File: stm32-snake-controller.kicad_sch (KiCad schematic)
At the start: 48 parts, among them J101 Barrel_Jack_MountingPin, J101 Tag Connector, J103 JST 2.54 Header, Q101 AO3501A, SW106 SW_Push, U101 STM32F446RCTx, U102 USBLC6-2SC6, U104 M24C64-RMN, Y101 16MHz, Y103 32.768kHz

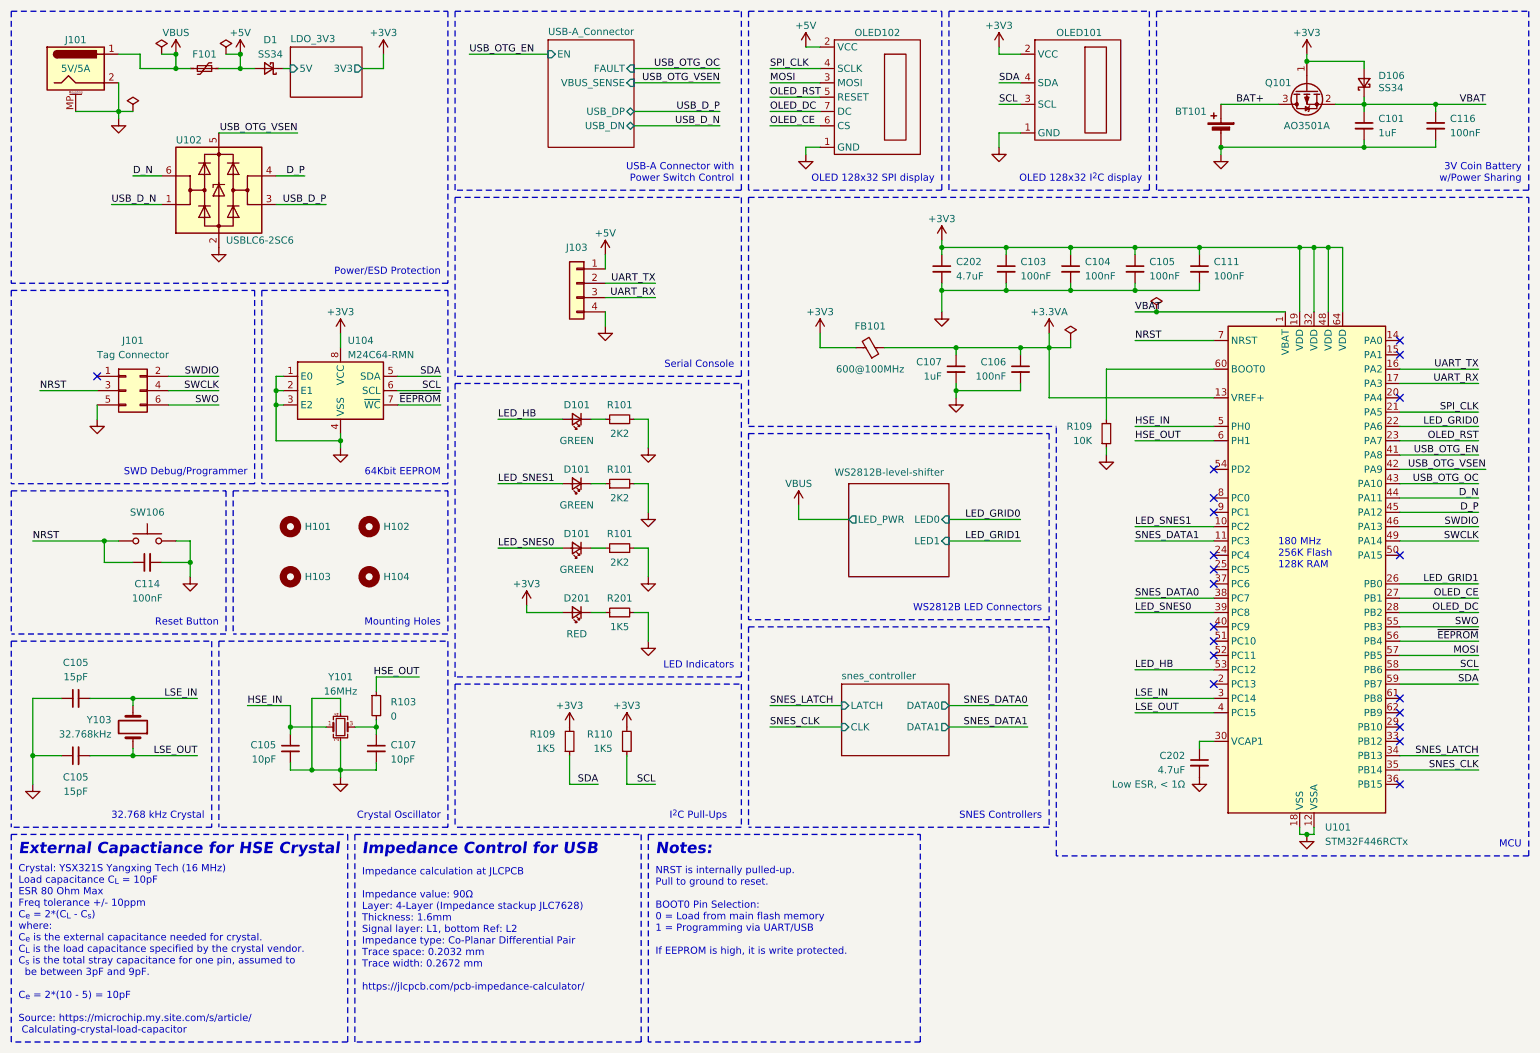
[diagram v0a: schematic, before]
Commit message: update schematic and pcb design to rev-b
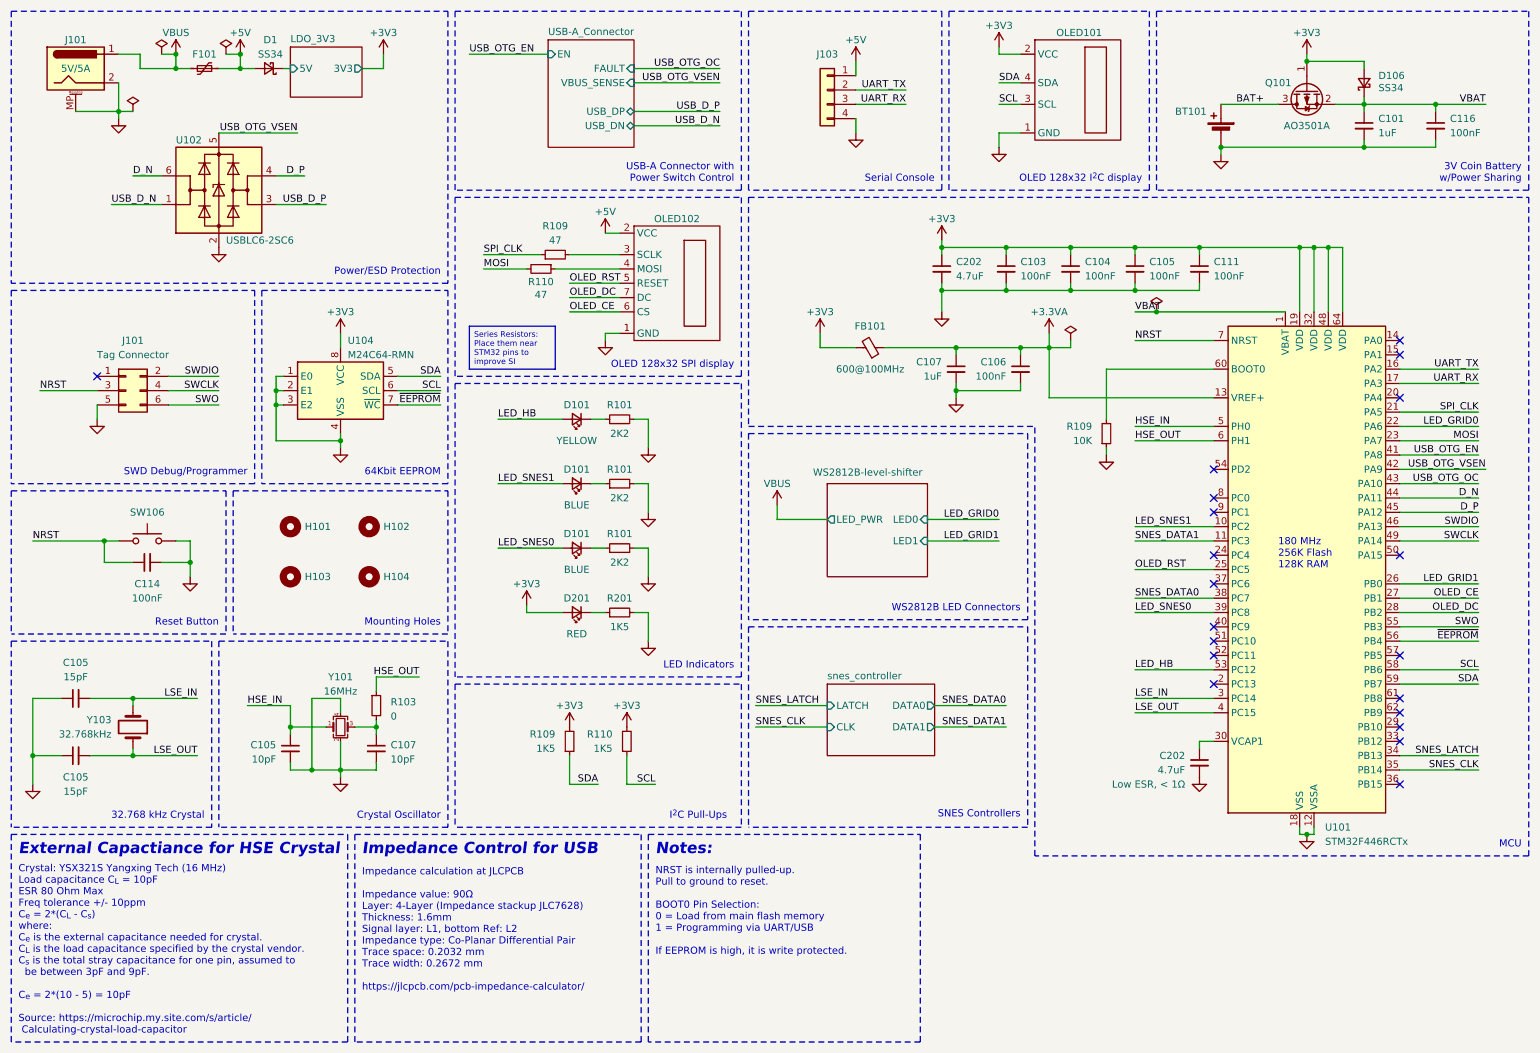
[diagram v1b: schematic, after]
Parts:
- added R109, R110: 47, Resistor_SMD:R_0603_1608Metric, symbol Device:R_Small
- D101: value GREEN -> BLUE; LCSC C72043 -> C965807
- D101: value GREEN -> YELLOW; LCSC C72043 -> C72038
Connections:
- net MOSI: now also U101.23 (PA7), R110.2; no longer OLED102.3 (MOSI), U101.57 (PB5)
- net OLED_RST: now also U101.25 (PC5); no longer U101.23 (PA7)
- net SPI_CLK: now also R109.1; no longer OLED102.4 (SCLK)
- new net: OLED102.3 (SCLK), R109.2
- new net: OLED102.4 (MOSI), R110.1
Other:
- moved on the sheet: J103, OLED102

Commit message: add power switch, rearrange pins for OLED display
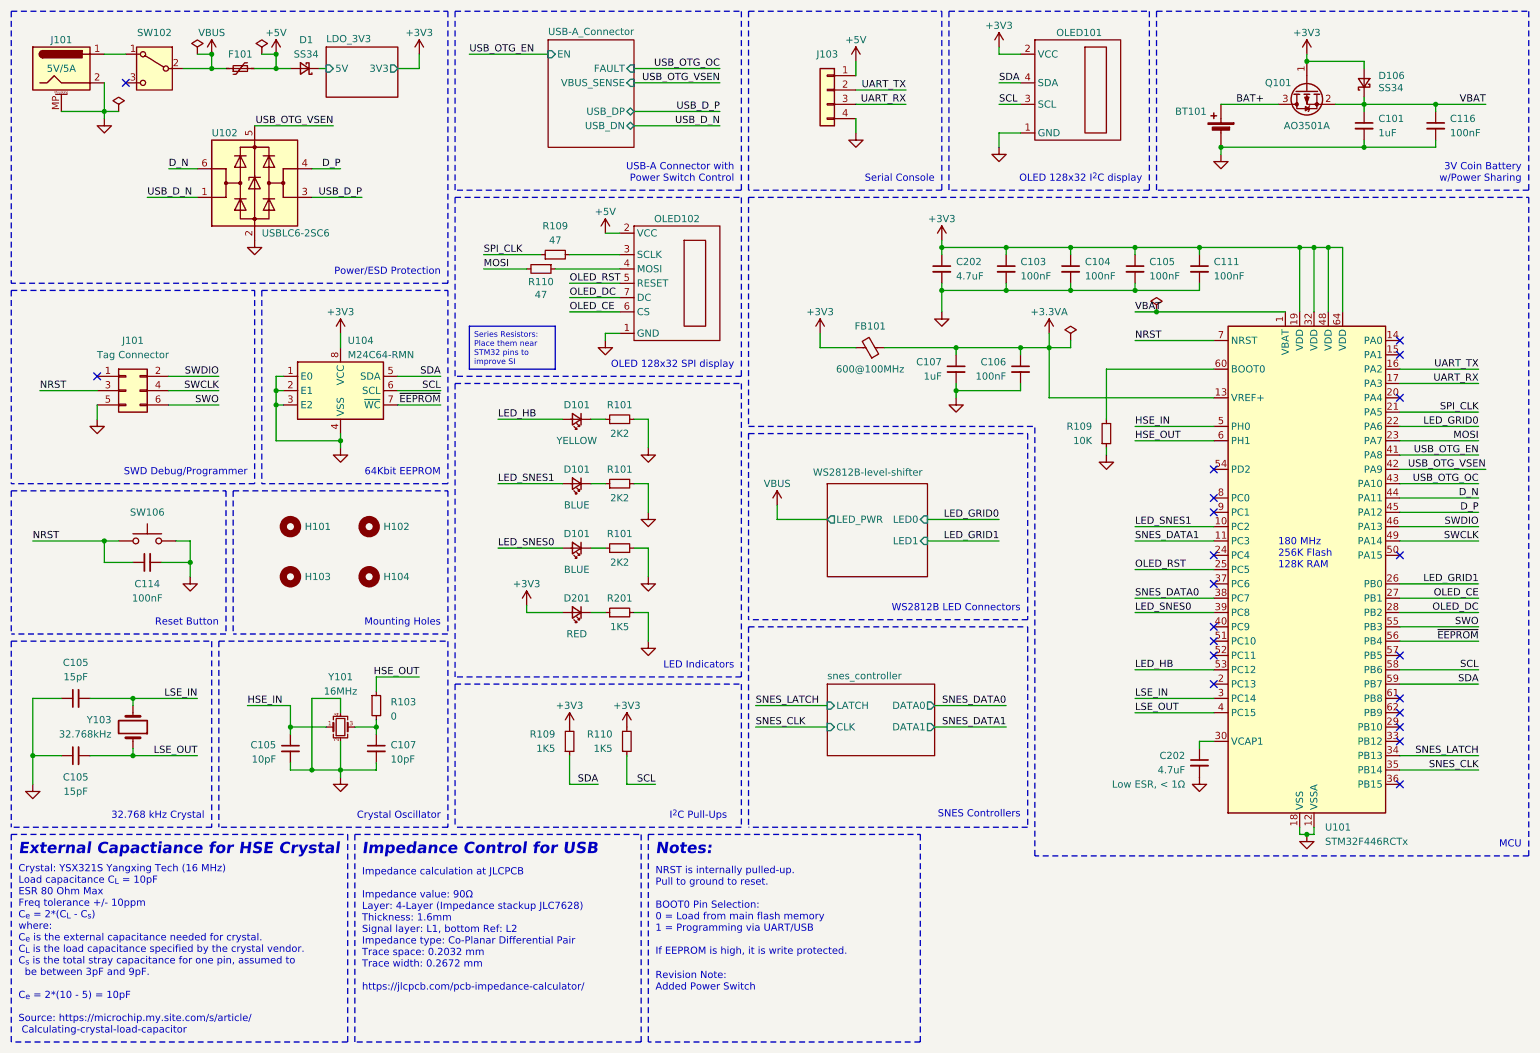
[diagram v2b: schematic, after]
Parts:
- added SW102: SW_SPDT, User_Footprint:Slide_Switch_SPDT_SS-12D06L5, symbol Switch:SW_SPDT
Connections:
- net VBUS: now also SW102.2 (B); no longer J101.1
- new net: J101.1, SW102.1 (A)
- no-connect marks 20 -> 21
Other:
- note added: "Revision Note: Added Power Switch"
- moved on the sheet: D1, F101, J101, U102

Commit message: add ferrite bead, 2nd i2c line, change power
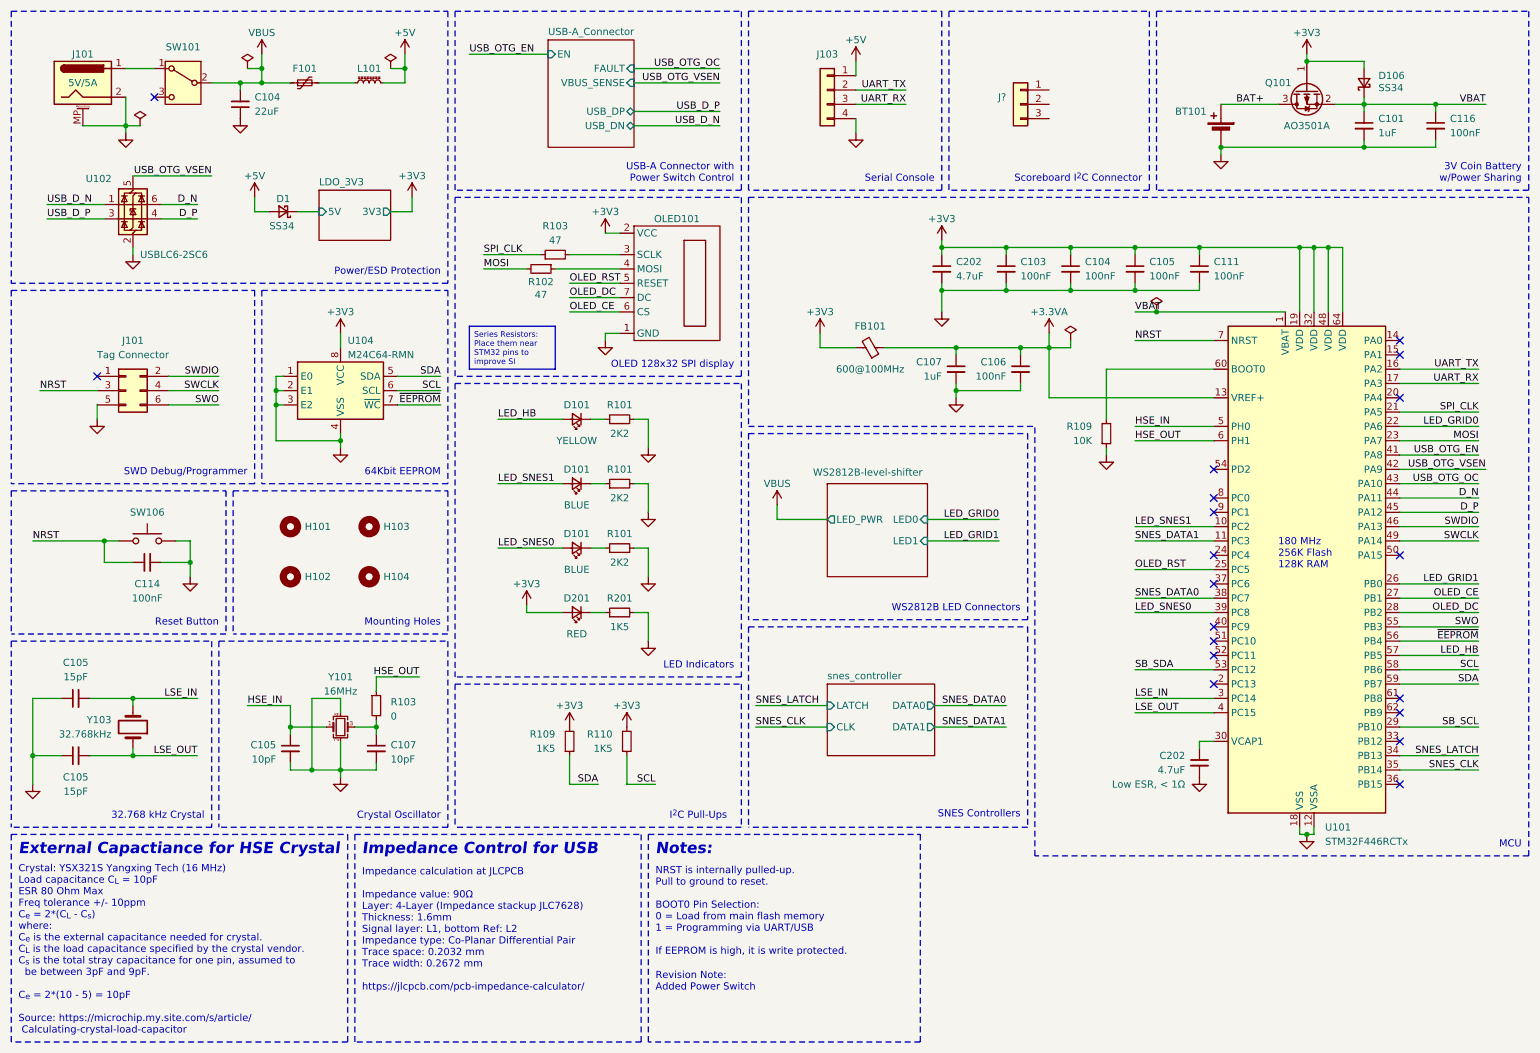
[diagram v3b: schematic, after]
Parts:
- removed OLED101: OLED_I2C, Connector_JST:JST_PH_B4B-PH-K_1x04_P2.00mm_Vertical, symbol User Symbols:OLED_I2C
- added C104: 22uF, Capacitor_SMD:C_0603_1608Metric, symbol Device:C_Small
- added J?: Conn_01x03, Connector_JST:JST_PH_B3B-PH-K_1x03_P2.00mm_Vertical, symbol Connector_Generic:Conn_01x03
- added L101: L_Ferrite_Small, Inductor_SMD:L_0603_1608Metric, symbol Device:L_Ferrite_Small
- renumbered H103 to H102, H102 to H103, OLED102 to OLED101, R110 to R102, R109 to R103, SW102 to SW101
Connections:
- net +3V3: now also OLED101.2 (VCC)
- net +5V: now also L101.2; no longer F101.2, OLED101.2 (VCC)
- net GND: now also C104.1
- net LED_HB: now also U101.57 (PB5); no longer U101.53 (PC12)
- net VBUS: now also C104.2
- net SB_SCL: now reaches U101.29 (PB10)
- new net: F101.2, L101.1
- new net SB_SDA: U101.53 (PC12)
- no-connect marks 21 -> 19
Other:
- note added: "Scoreboard I^{2}C Connector"
- note removed: "OLED 128x32 I^{2}C display"
- moved on the sheet: D1, F101, J101, SW101

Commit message: add scoreboard connector
- add ethernet jack for scoreboard connection
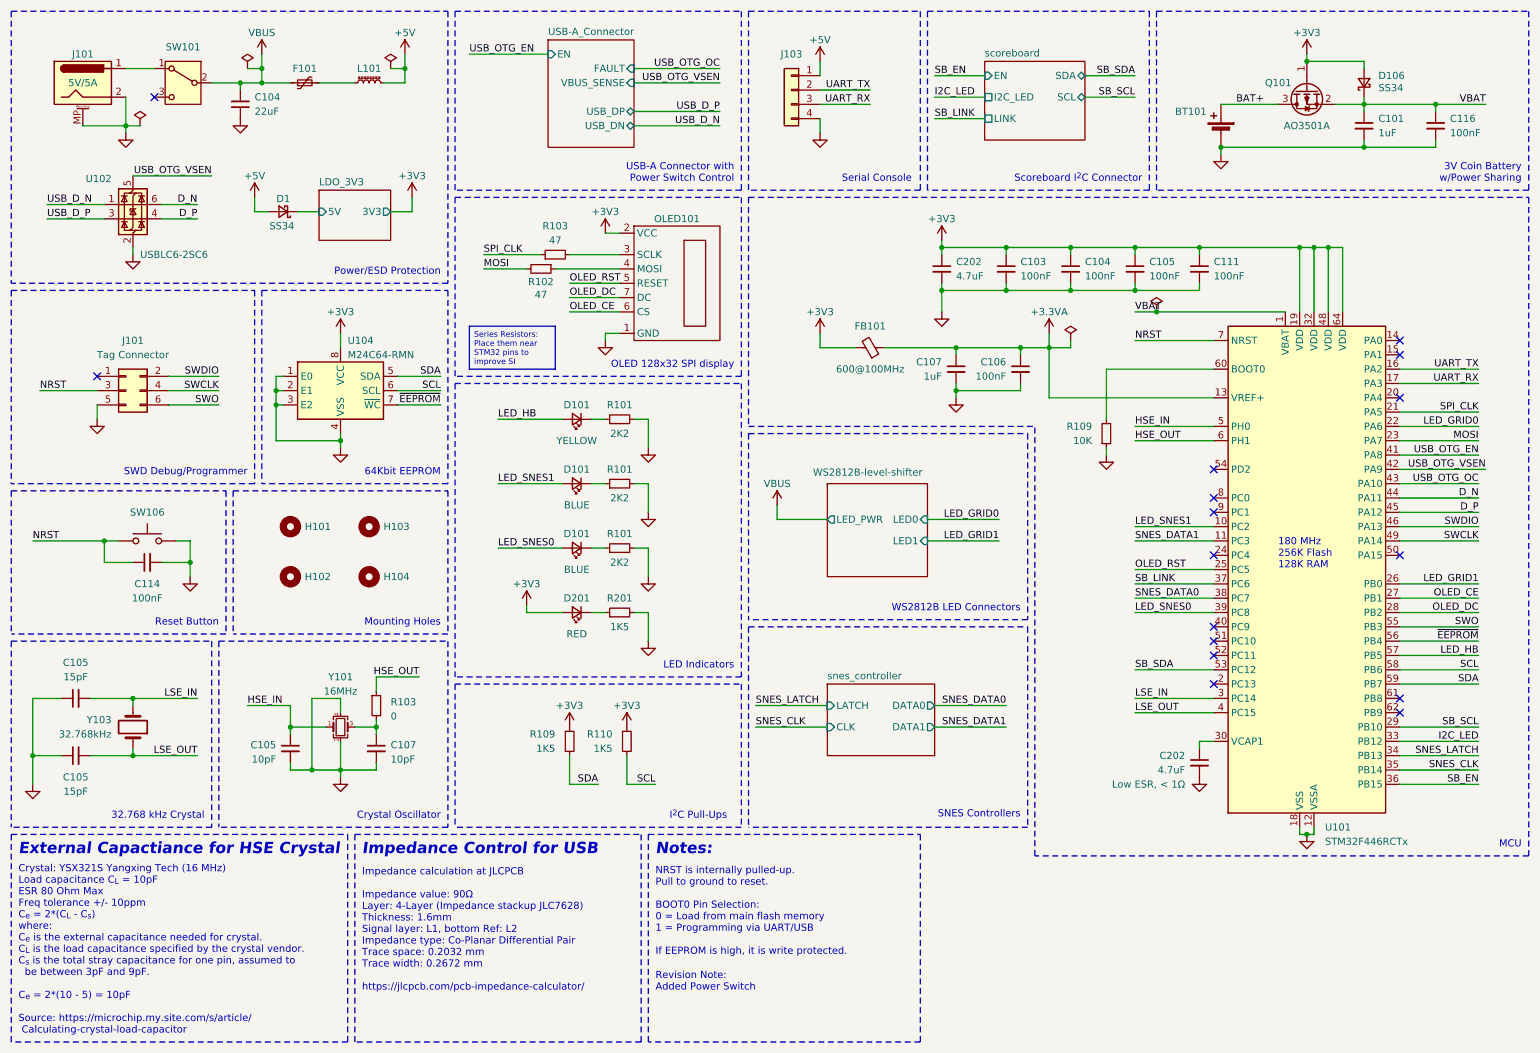
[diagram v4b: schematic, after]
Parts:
- removed J?: Conn_01x03, Connector_JST:JST_PH_B3B-PH-K_1x03_P2.00mm_Vertical, symbol Connector_Generic:Conn_01x03
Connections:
- net I2C_LED: now reaches U101.33 (PB12)
- net SB_EN: now reaches U101.36 (PB15)
- net SB_LINK: now reaches U101.37 (PC6)
- no-connect marks 19 -> 16
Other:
- added sheet scoreboard (scoreboard.kicad_sch)
- moved on the sheet: J103

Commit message: remove pull-down resistor
- The original schematic had pull-down resistors for link detection, after a breadboard testing, it failed. Looked at the oscilloscope, it showed that the signal voltage dropped,  acting like a voltage divider so the line did not get pulled down to 0V. Removing the resistor fixed that.
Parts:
- SW101: LCSC C319015 -> C319015
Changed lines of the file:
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@@
 			)
 		)
-		(property "LCSC" " C319015"
+		(property "LCSC" "C319015"
 			(at 44.45 26.67 0)
 			(effects

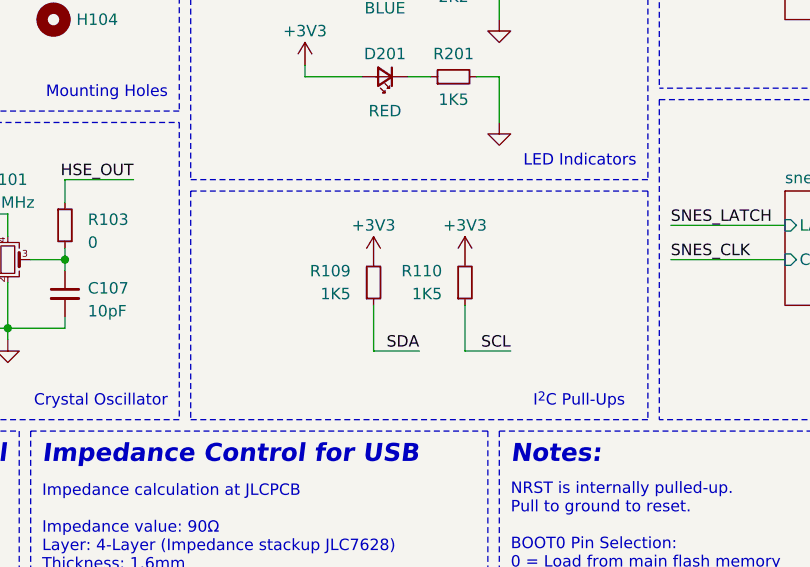
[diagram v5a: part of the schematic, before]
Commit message: add pull-up resistor for 2nd I2C lines
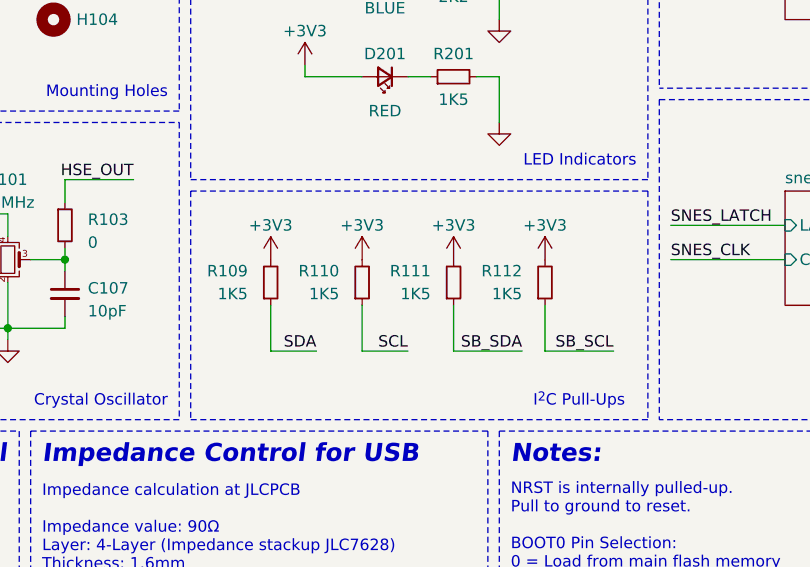
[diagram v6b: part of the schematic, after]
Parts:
- added R111, R112: 1K5, Resistor_SMD:R_0603_1608Metric, symbol Device:R_Small
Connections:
- net +3V3: now also R111.2, R112.2
- net SB_SCL: now also R112.1
- net SB_SDA: now also R111.1
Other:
- moved on the sheet: R109, R110
